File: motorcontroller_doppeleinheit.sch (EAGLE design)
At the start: 21 parts

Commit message: ...
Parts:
- removed QG1: 16,384Mhz, crystal:QG5860
- added C3, C4: 22pF, rcl:C-EUC1206
- added Q1: 16,384Mhz, crystal:CRYSTALHC49UP
- added R3: 10k, rcl:R-EU_R1206
- C1: device rcl:C-EU075-032X103 -> rcl:C-EUC1206
- R1: device rcl:R-EU_0207/12 -> rcl:C-EUC1206
- R2: device rcl:R-EU_0207/12 -> rcl:R-EU_R1206
- U$1: value TINY2313-*P* -> TINY2313-*S*; device avr-7:TINY2313-*P* -> avr-7:TINY2313-*S*
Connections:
- new net N$5: C3.2, Q1.2, U$1.PA1(XTAL2)
- net +5V: now also R3.2; no longer QG1.VCC
- net GND: now also C3.1, C4.1; no longer QG1.GND
- net LOCKED: now also R3.1
- net N$1: now also C4.2, Q1.1; no longer QG1.OUT
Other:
- moved on the sheet: R1, R2

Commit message: ...
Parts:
- removed RESET: (no value), switch-omron:10-XX
- ISP: device con-ml:ML6 -> con-harting-ml:ML6L
- R1: device rcl:C-EUC1206 -> rcl:R-EU_R1206
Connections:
- net GND: no longer RESET.P, RESET.P1
- net RST: no longer RESET.S, RESET.S1
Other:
- moved on the sheet: R1
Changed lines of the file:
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@@
 <part name="PHOTO1" library="_custom_con" deviceset="FLAT_P4" device=""/>
 <part name="U$1" library="avr-7" deviceset="TINY2313*" device="-*S*" value="TINY2313-*S*"/>
-<part name="R1" library="rcl" deviceset="C-EU" device="C1206" value="10k"/>
+<part name="R1" library="rcl" deviceset="R-EU_" device="R1206" value="10k"/>
 <part name="R2" library="rcl" deviceset="R-EU_" device="R1206" value="390"/>
 <part name="P+2" library="supply1" deviceset="+5V" device=""/>
@@
 <part name="GND2" library="supply1" deviceset="GND" device=""/>
 <part name="C1" library="rcl" deviceset="C-EU" device="C1206" value="100nF"/>
-<part name="RESET" library="switch-omron" deviceset="10-XX" device=""/>
-<part name="GND3" library="supply1" deviceset="GND" device=""/>
 <part name="U$2" library="diy-modules" deviceset="DC-DC-STEP-UP-MT3608" device=""/>
 <part name="P+5" library="supply1" deviceset="+24V" device=""/>
@@
 <part name="P+13" library="supply1" deviceset="+5V" device=""/>
 <part name="FRAME1" library="frames" deviceset="DINA4_L" device=""/>
-<part name="ISP" library="con-ml" deviceset="ML6" device=""/>
+<part name="ISP" library="con-harting-ml" deviceset="ML6" device="L"/>
 <part name="LASER1" library="jumper" deviceset="JP1Q" device=""/>
 <part name="LASER2" library="jumper" deviceset="JP1Q" device=""/>
@@
 </instance>
 <instance part="U$1" gate="G$1" x="157.48" y="99.06"/>
-<instance part="R1" gate="G$1" x="134.62" y="119.38" rot="R180"/>
+<instance part="R1" gate="G$1" x="134.62" y="121.92" rot="R90"/>
 <instance part="R2" gate="G$1" x="154.94" y="149.86"/>
 <instance part="P+2" gate="1" x="134.62" y="129.54"/>
@@
 <instance part="GND2" gate="1" x="137.16" y="66.04"/>
 <instance part="C1" gate="G$1" x="137.16" y="73.66" rot="R180"/>
-<instance part="RESET" gate="1" x="121.92" y="119.38" rot="R270"/>
-<instance part="GND3" gate="1" x="116.84" y="114.3"/>
 <instance part="U$2" gate="G$1" x="193.04" y="149.86" rot="MR0"/>
 <instance part="P+5" gate="1" x="218.44" y="157.48"/>
@@
 <pinref part="R1" gate="G$1" pin="1"/>
 <wire x1="134.62" y1="116.84" x2="137.16" y2="116.84" width="0.1524" layer="91"/>
-<pinref part="RESET" gate="1" pin="S"/>
-<pinref part="RESET" gate="1" pin="S1"/>
-<wire x1="127" y1="119.38" x2="127" y2="116.84" width="0.1524" layer="91"/>
-<wire x1="127" y1="116.84" x2="134.62" y2="116.84" width="0.1524" layer="91"/>
-<junction x="127" y="116.84"/>
-<junction x="134.62" y="116.84"/>
 </segment>
 </net>
@@
 <pinref part="C1" gate="G$1" pin="1"/>
 <junction x="137.16" y="71.12"/>
-</segment>
-<segment>
-<pinref part="RESET" gate="1" pin="P"/>
-<pinref part="RESET" gate="1" pin="P1"/>
-<wire x1="116.84" y1="119.38" x2="116.84" y2="116.84" width="0.1524" layer="91"/>
-<pinref part="GND3" gate="1" pin="GND"/>
-<junction x="116.84" y="116.84"/>
 </segment>
 <segment>
@@
 <pinref part="R1" gate="G$1" pin="2"/>
 <pinref part="P+2" gate="1" pin="+5V"/>
-<wire x1="134.62" y1="127" x2="134.62" y2="124.46" width="0.1524" layer="91"/>
-</segment>
-<segment>
+</segment>
+<segment>

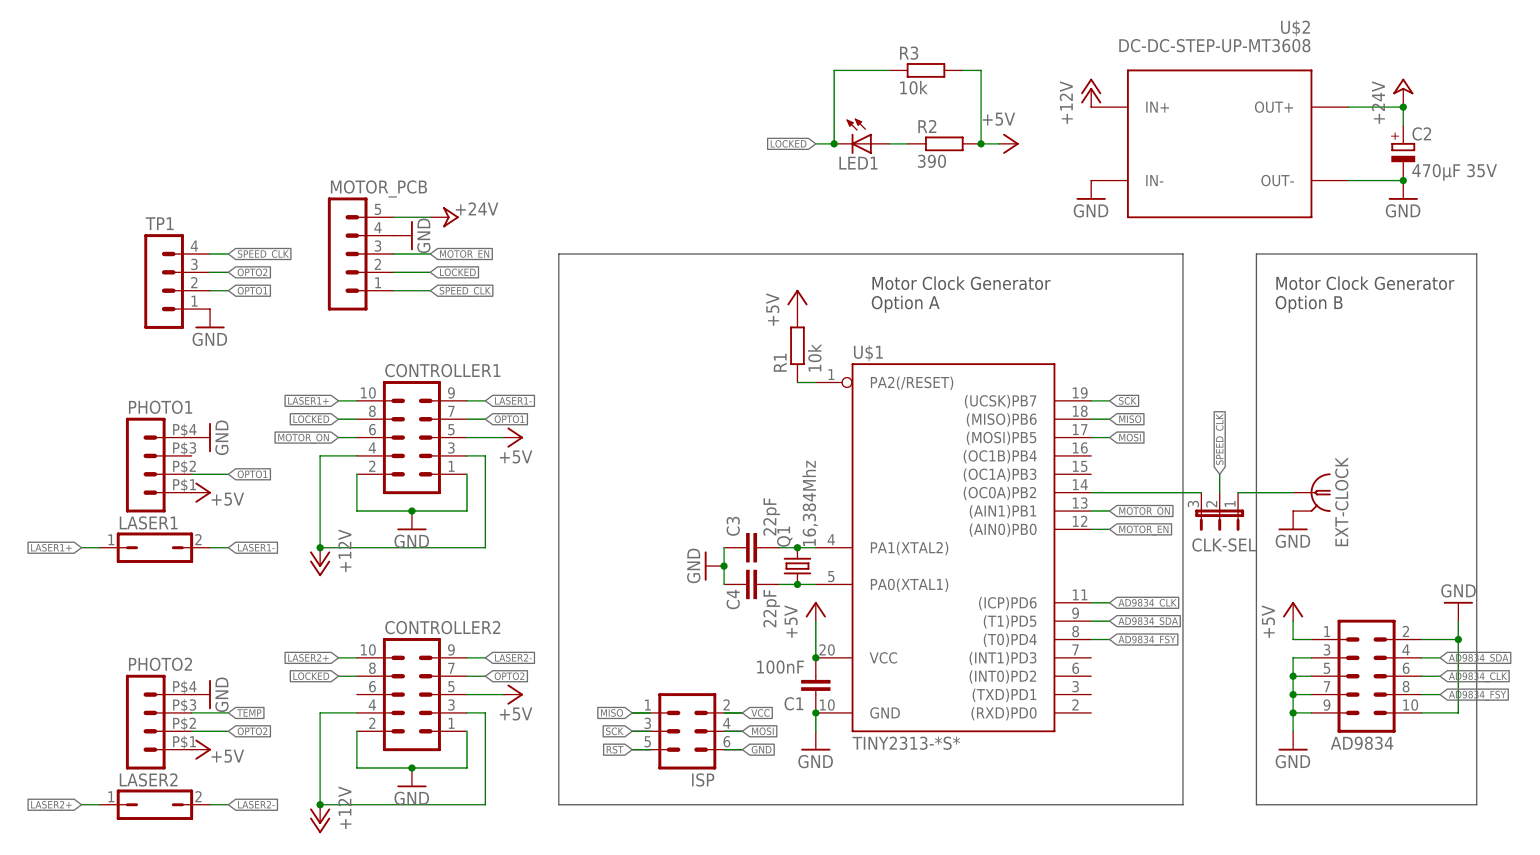
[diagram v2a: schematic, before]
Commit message: Added C5, modified firmware because of inverted logic
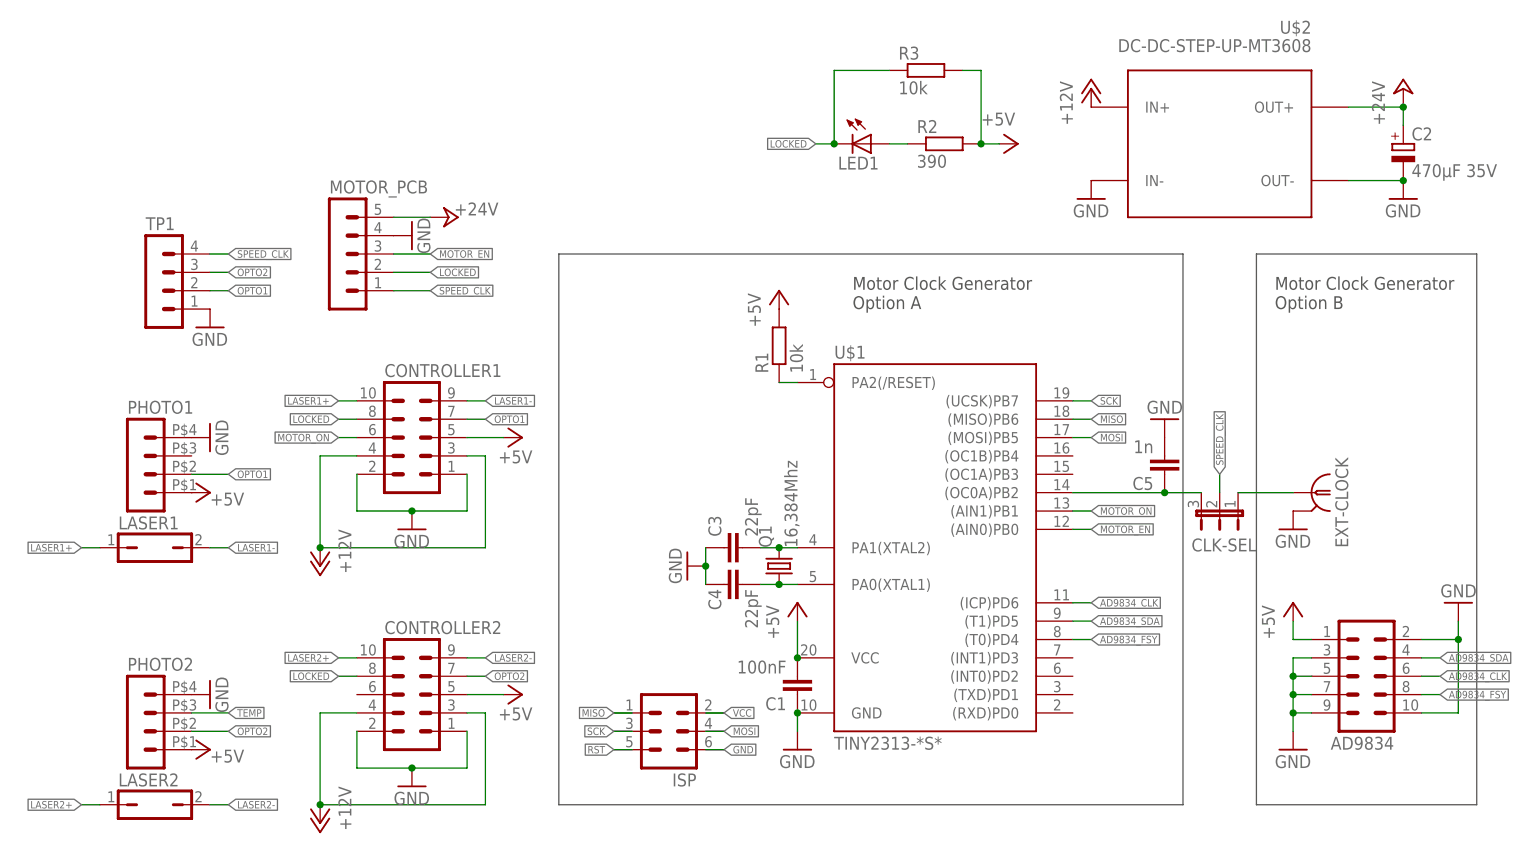
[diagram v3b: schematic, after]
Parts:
- added C5: 1n, rcl:C-EUC1206
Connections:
- net GND: now also C5.2
- net N$3: now also C5.1
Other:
- moved on the sheet: C1, C3, C4, ISP, Q1, R1, U$1
